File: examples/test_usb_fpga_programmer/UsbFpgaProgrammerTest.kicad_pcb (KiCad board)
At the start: 2 copper layers, 52 x 18 mm, 40 parts

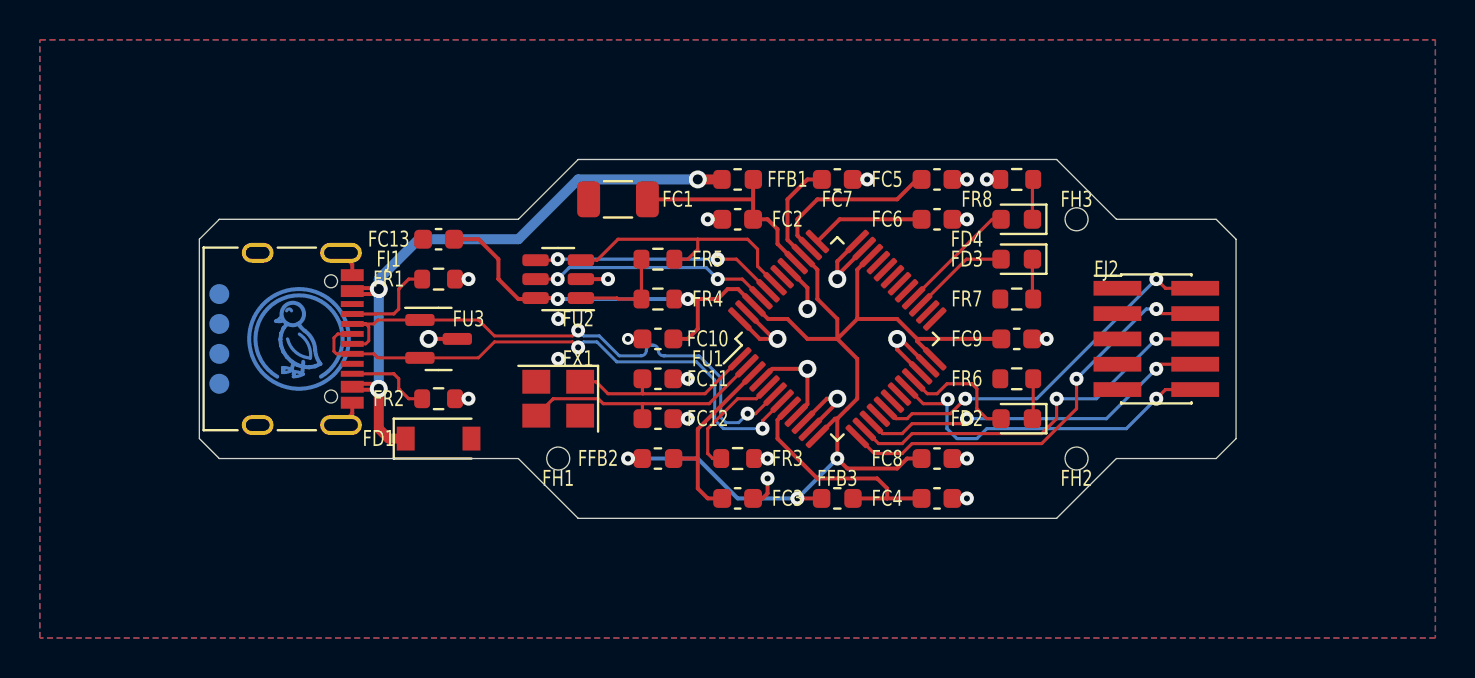
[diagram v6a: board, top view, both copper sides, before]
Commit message: layout cleanup + recoloring
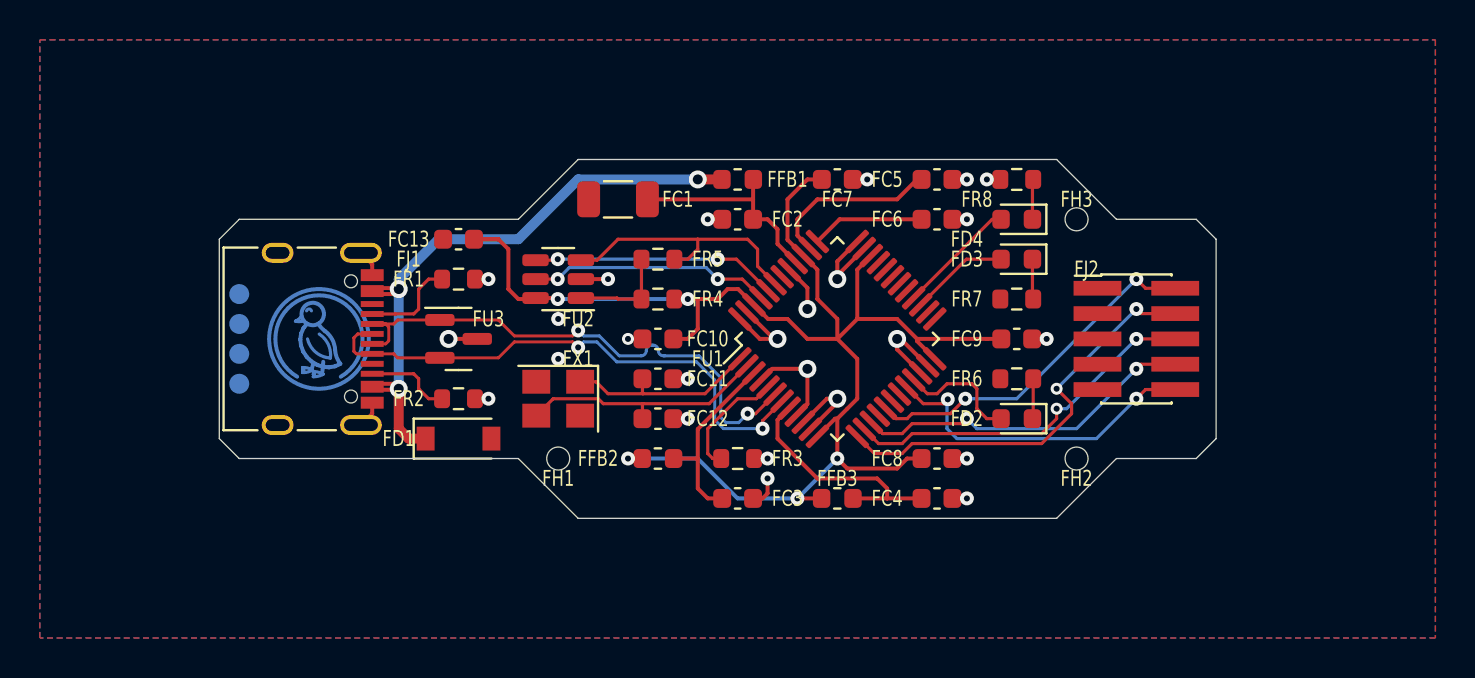
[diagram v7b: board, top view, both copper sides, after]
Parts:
- FD4: value KT-0603R (Hubei KENTO Elec) - Red 615~630nm 1.9~2.2V 0603 Light Emitting Diodes (LED) RoHS -> (none)
- moved FC13 1.00 mm to (119.0, 43.0)
- moved FD1 1.00 mm to (119.0, 53.0)
- moved FJ1 1.00 mm to (111.0, 48.0)
- moved FJ2 1.00 mm to (153.0, 48.0)
- moved FR1 1.00 mm to (119.0, 45.0)
- moved FR2 1.00 mm to (119.0, 51.0)
- moved FU3 1.00 mm to (119.0, 48.0)
- moved FU4 1.00 mm to (112.0, 48.0)
- moved FU5 1.00 mm to (117.0, 48.0)
- moved FU6 1.00 mm to (108.0, 48.0)
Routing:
- net ft232.mpsse.mosi: track 19.7 -> 18.4 mm
- net ft232.adbus7: track 17.7 -> 16.7 mm
- net vusb: track 33.8 -> 32.8 mm
- net usb_chain_0.d_N: track 28.5 -> 27.5 mm
- net ft232.adbus4: track 18.8 -> 17.8 mm
- net usb_chain_0.d_P: track 28.7 -> 27.7 mm
- net ft232.ic.vccd: track 76.9 -> 77.4 mm
- net ft232.mpsse.miso: track 17.9 -> 17.3 mm
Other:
- board size 52 x 18 mm -> 50 x 18 mm
